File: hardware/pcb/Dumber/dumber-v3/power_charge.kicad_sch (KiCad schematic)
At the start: 44 parts, among them P1 USB_C_Plug_GCT_USB4125, Q1 PMN52XP, SW1 SW_Push, U3 LTC2954-2, U4 L6924U, U5 LM2731XMF, U6 AP2206

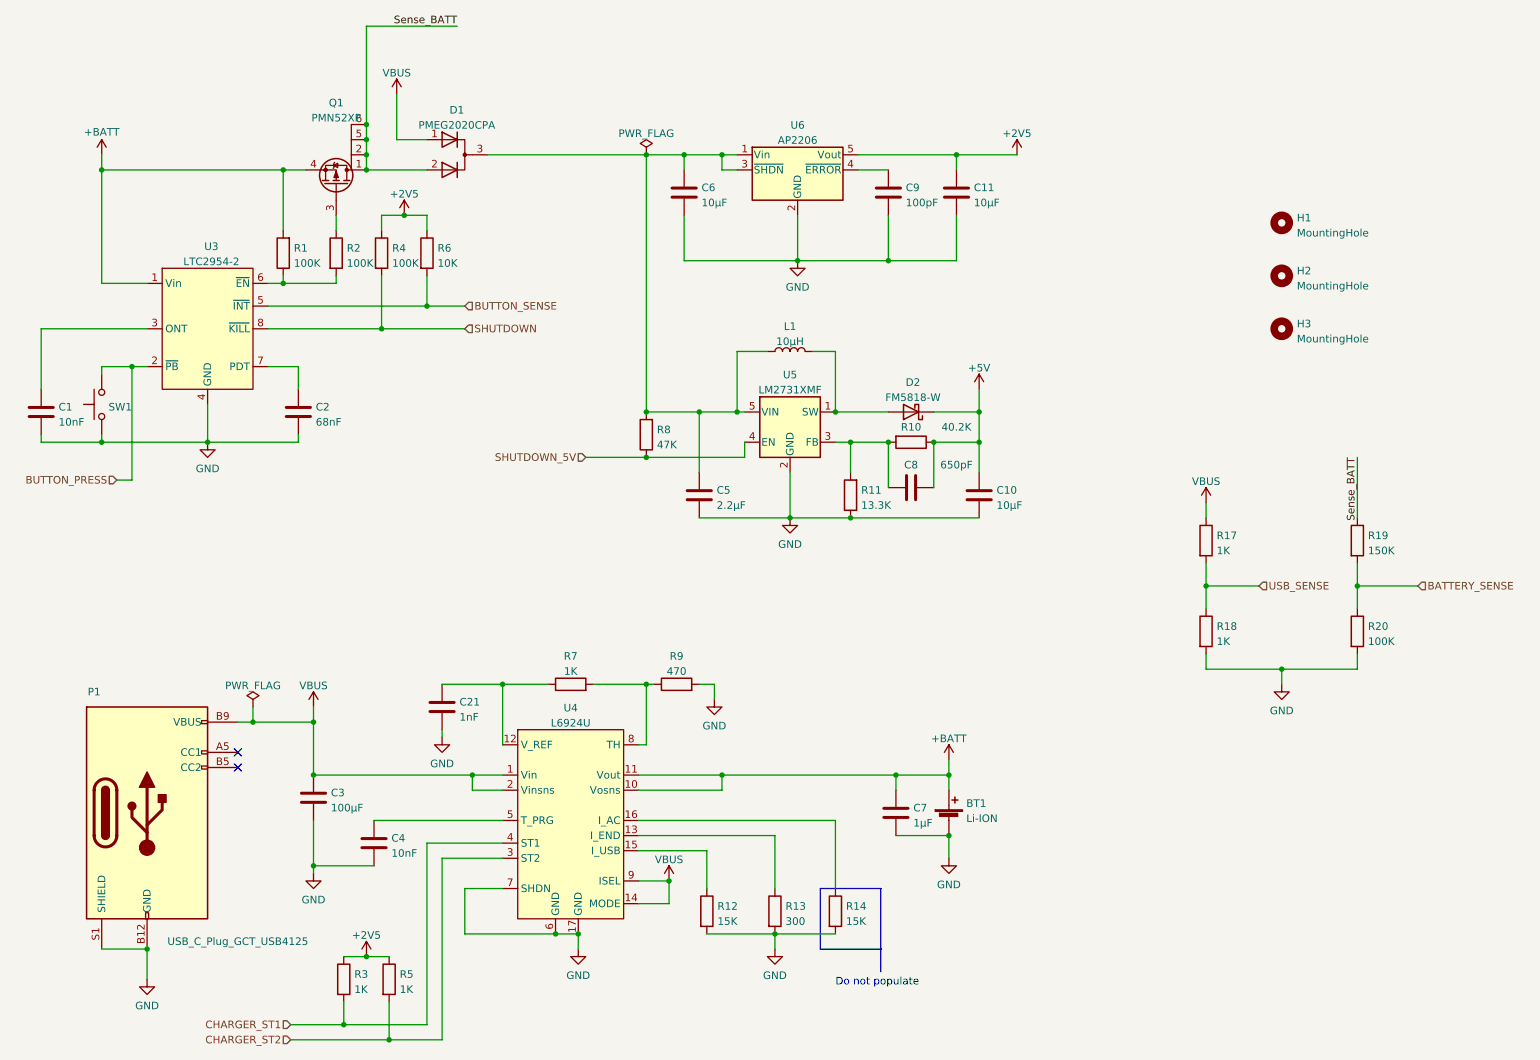
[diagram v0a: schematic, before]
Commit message: Corrections autour des zones a activer ou deactiver en fonction de l'etat de connexion
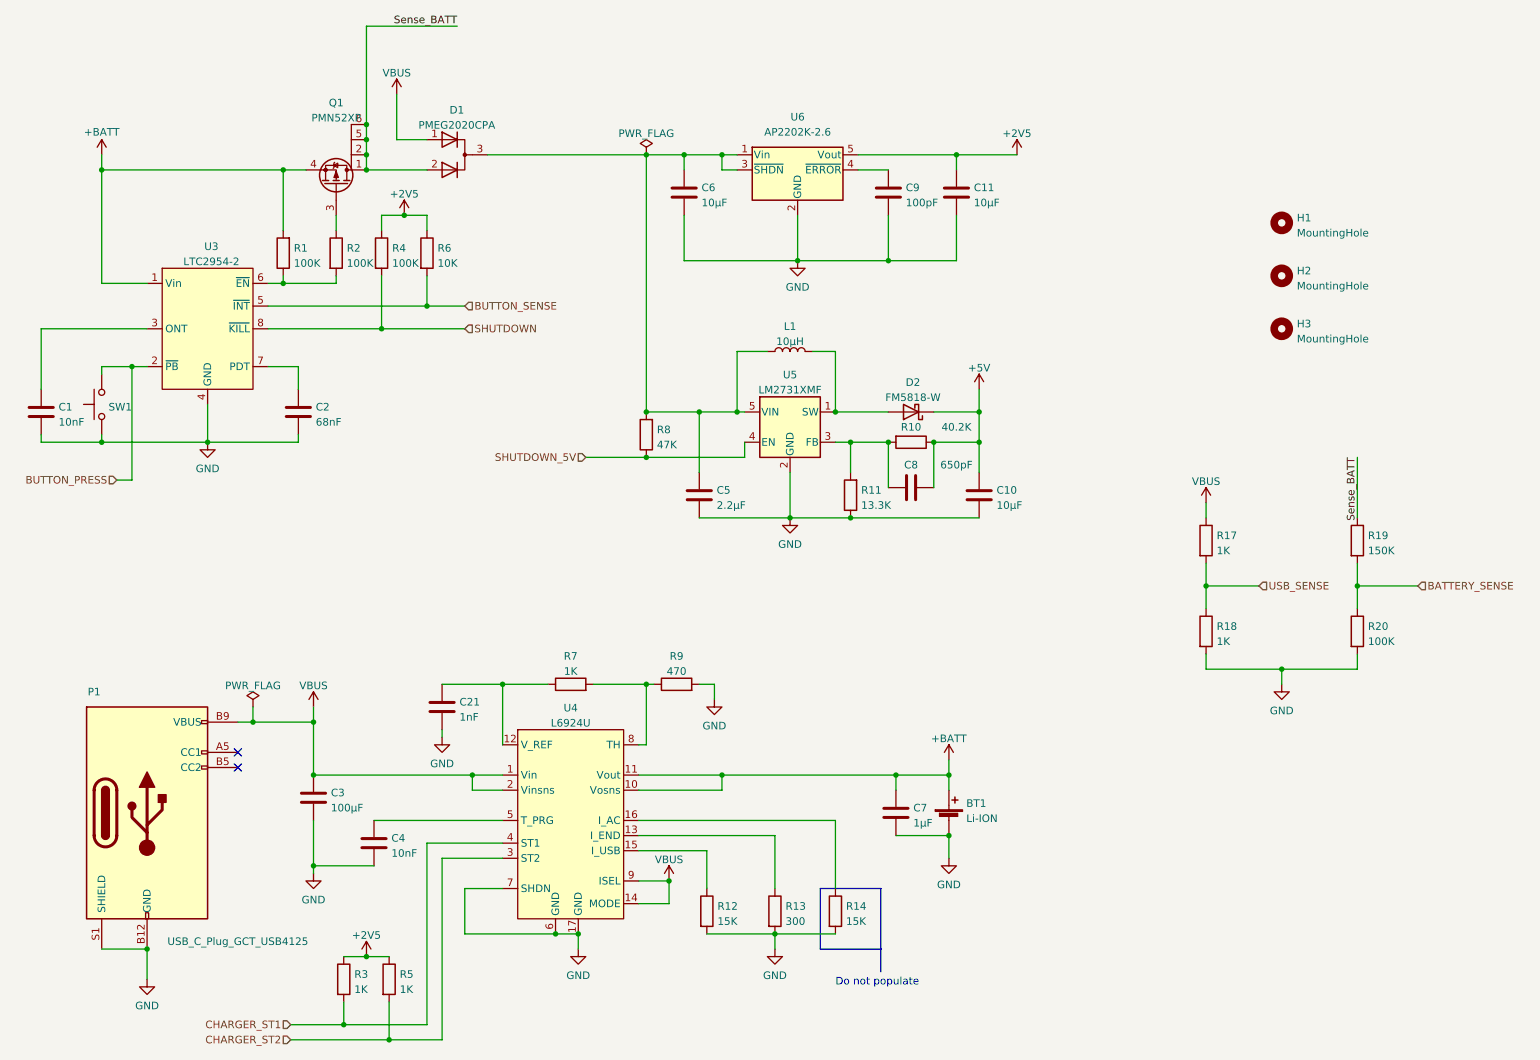
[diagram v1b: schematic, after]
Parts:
- U6: value AP2206 -> AP2202K-2.6
